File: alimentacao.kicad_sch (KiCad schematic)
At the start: 8 parts

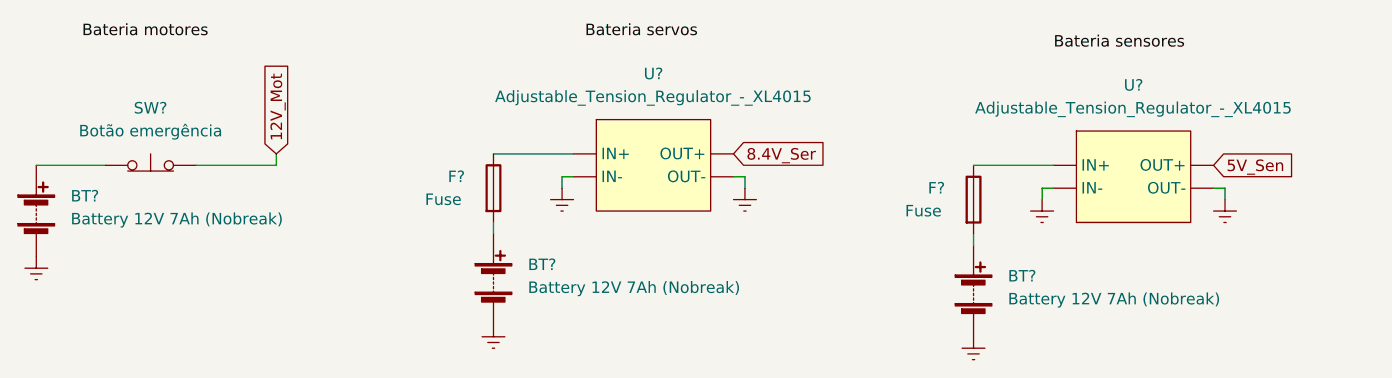
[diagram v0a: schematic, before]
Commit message: fix: modificado saídas do arduino
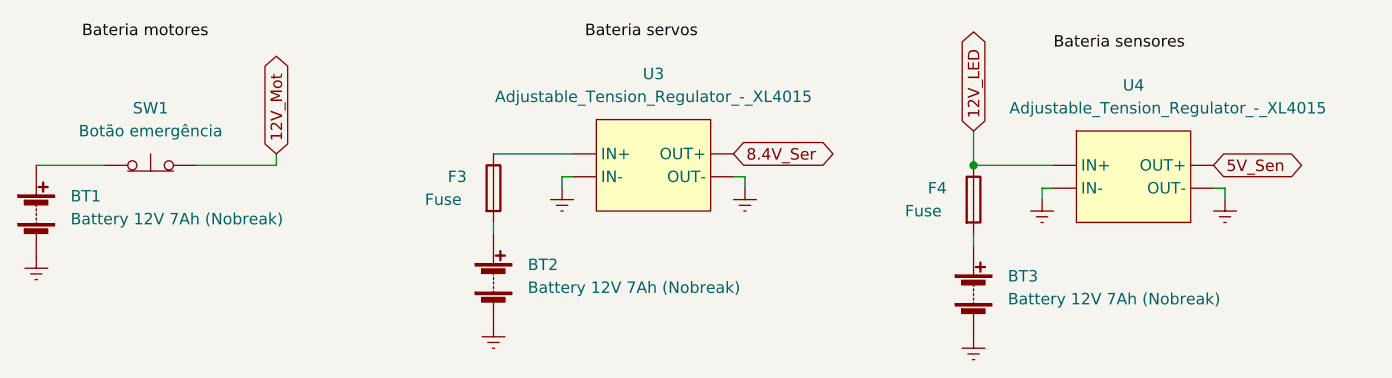
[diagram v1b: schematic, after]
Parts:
- BT1, BT2, BT3: renamed from BT?; footprint (none) -> TerminalBlock_Phoenix:TerminalBlock_Phoenix_MKDS-1,5-2_1x02_P5.00mm_Horizontal
- U3, U4: renamed from U?; footprint (none) -> TerminalBlock_Phoenix:TerminalBlock_Phoenix_MKDS-1,5-2-5.08_1x02_P5.08mm_Horizontal
- gave numbers to parts that had none: 3
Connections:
- net 12V_LED: now reaches F4.1, U4. (OUT-)
